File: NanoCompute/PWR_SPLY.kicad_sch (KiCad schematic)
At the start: 3 parts, among them U5 TPS54308, U7 TLV74311, U8 TLV74325

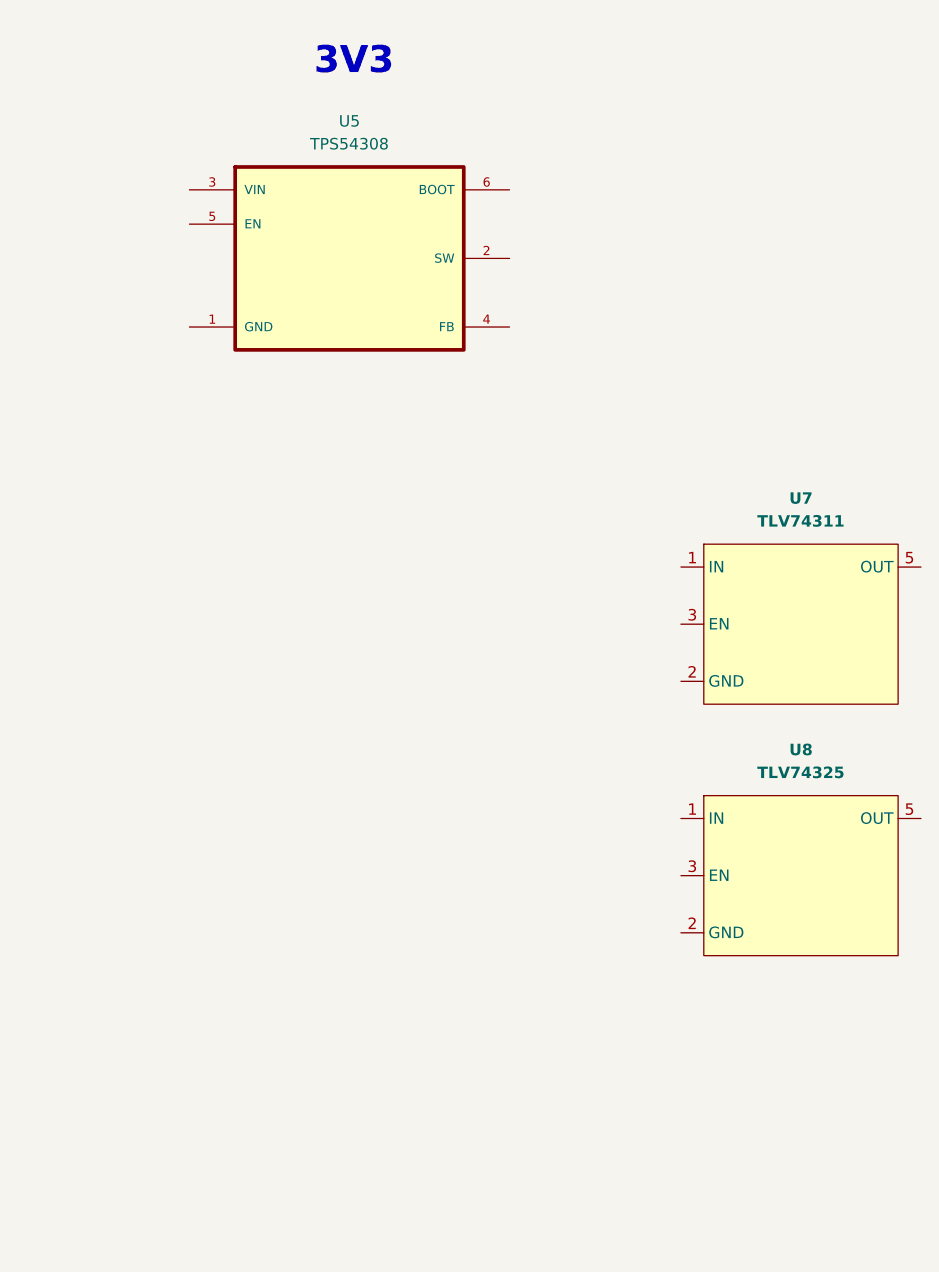
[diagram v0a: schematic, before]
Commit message: LPDDR4 second chip connected to LPDDR4 PHY
Added a missing Units for second LPDDR4 chip (VSS and Power).
Added a 1x100nF decoupling capacitor for each power rail of VDD1 but it
seems too much. Might need to find a better way of doing Low-Mid-High
range frequency decoupling.
Added TPS65296 as a LPddr4 Memory power solution but I need to check if
I can power both memory chips with just one TPS65296.
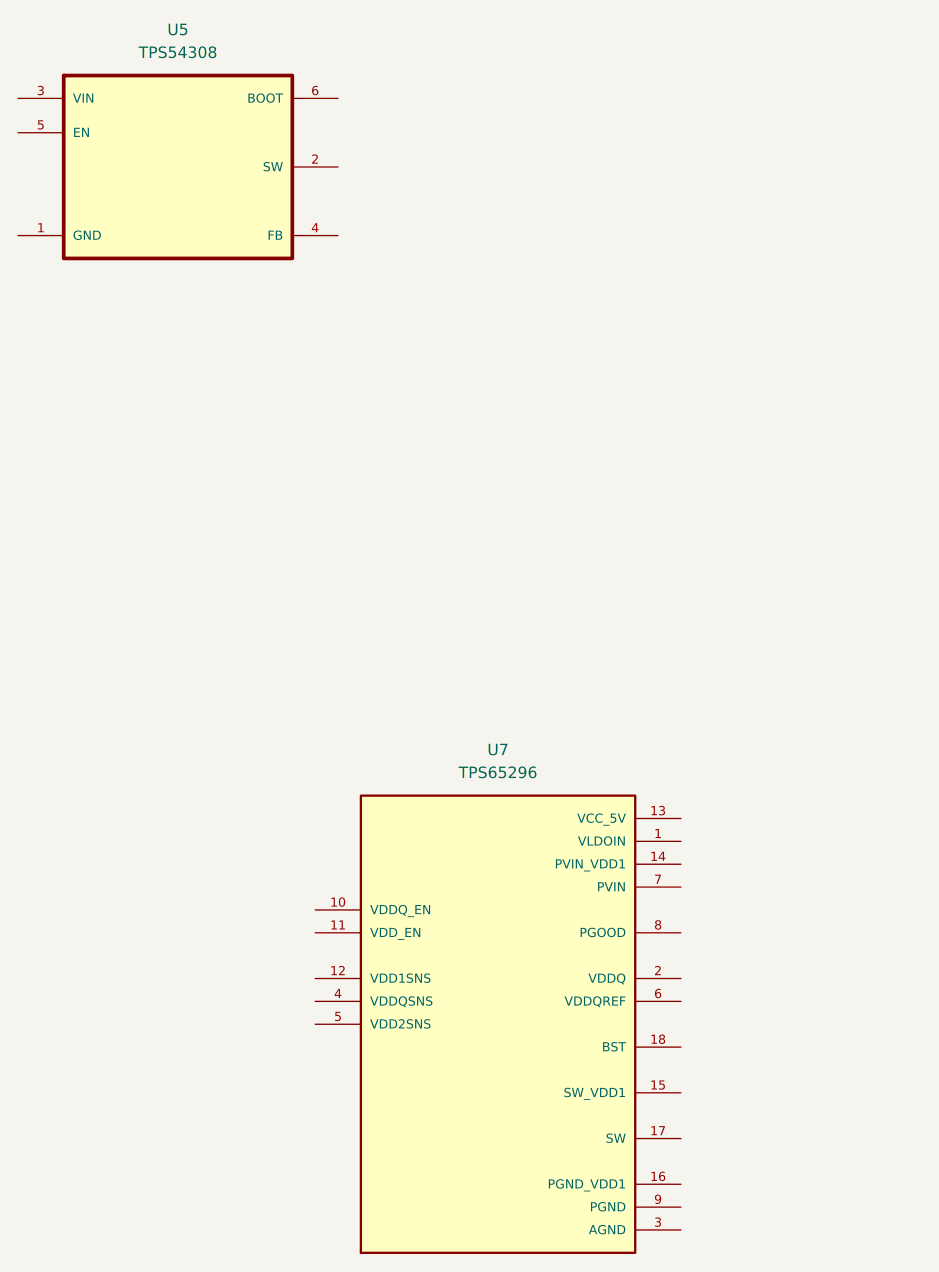
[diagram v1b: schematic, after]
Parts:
- removed U7: TLV74311, Package_TO_SOT_SMD:SOT-23-5, symbol CBSymLib:TLV743-11
- removed U8: TLV74325, Package_TO_SOT_SMD:SOT-23-5, symbol CBSymLib:TLV743-25
- added U7: TPS65296, CBFtLib:TPS65296RJER, symbol CBSymLib:TPS65296RJER
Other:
- note removed: "3V3"
- moved on the sheet: U5
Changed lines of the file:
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@@
 		(rev "v1.0")
 	)
-	(text "3V3"
-		(exclude_from_sim no)
-		(at 58.928 21.336 0)
-		(effects
-			(font
-				(size 3 3)
-				(thickness 0.6)
-				(bold yes)
-			)
-		)
-	)
 	(symbol
-		(lib_id "CBSymLib:TLV743-25")
-		(at 107.95 105.41 0)
+		(lib_id "CBSymLib:TPS65296RJER")
+		(at 74.93 128.27 0)
 		(unit 1)
 		(exclude_from_sim no)
@@
 		(on_board yes)
 		(dnp no)
-		(property "Reference" "U8"
-			(at 108.585 97.79 0)
+		(fields_autoplaced yes)
+		(property "Reference" "U7"
+			(at 74.93 97.79 0)
 			(effects
 				(font
 					(size 1.27 1.27)
-					(thickness 0.254)
-					(bold yes)
 				)
 			)
 		)
-		(property "Value" "TLV74325"
-			(at 108.585 100.33 0)
+		(property "Value" "TPS65296"
+			(at 74.93 100.33 0)
 			(effects
 				(font
 					(size 1.27 1.27)
-					(thickness 0.254)
-					(bold yes)
 				)
 			)
 		)
-		(property "Footprint" "Package_TO_SOT_SMD:SOT-23-5"
-			(at 107.95 105.41 0)
+		(property "Footprint" "CBFtLib:TPS65296RJER"
+			(at 74.93 128.27 0)
+			(effects
+				(font
+					(size 1.27 1.27)
+				)
+				(justify bottom)
+				(hide yes)
+			)
+		)
+		(property "Datasheet" "https://www.ti.com/general/docs/suppproductinfo.tsp?distId=10&gotoUrl=https%3A%2F%2Fwww.ti.com%2Flit%2Fgpn%2Ftps65296"
+			(at 74.93 128.27 0)
 			(effects
 				(font
@@
 			)
 		)
-		(property "Datasheet" "https://www.ti.com/general/docs/suppproductinfo.tsp?distId=10&gotoUrl=https%3A%2F%2Fwww.ti.com%2Flit%2Fgpn%2Ftlv743p"
-			(at 107.95 105.41 0)
+		(property "Description" "Converter, Notebook Power System Voltage Regulator IC 2 Output 18-VQFN-HR (3x3)"
+			(at 74.93 128.27 0)
 			(effects
 				(font
@@
 			)
 		)
-		(property "Description" "Linear Voltage Regulator IC Positive Fixed 1 Output 300mA SOT-23-5"
-			(at 107.95 105.41 0)
+		(property "Digikey stock" "5,921 - 4/1/2024"
+			(at 74.93 128.27 0)
 			(effects
 				(font
@@
 			)
 		)
-		(property "Digikey stock" "17,002 - 29/12/2024"
-			(at 107.95 105.41 0)
-			(effects
-				(font
-					(size 1.27 1.27)
-				)
-				(hide yes)
-			)
-		)
-		(property "MPN" "TLV74325PDBVR"
-			(at 107.95 105.41 0)
-			(effects
-				(font
-					(size 1.27 1.27)
-				)
-				(hide yes)
-			)
-		)
-		(pin "3"
-		)
-		(pin "1"
-		)
-		(pin "4"
-		)
-		(pin "5"
-		)
-		(pin "2"
-		)
-		(instances
-			(project "CuriosityBoard"
-				(path "/3a0a6fc3-d957-4804-b3c3-6d269c038b1f/d23503c1-e384-4c86-8da8-7bc1f5bc6ede"
-					(reference "U8")
-					(unit 1)
-				)
-			)
-		)
-	)
-	(symbol
-		(lib_id "CBSymLib:TLV743-11")
-		(at 107.95 77.47 0)
-		(unit 1)
-		(exclude_from_sim no)
-		(in_bom yes)
-		(on_board yes)
-		(dnp no)
-		(property "Reference" "U7"
-			(at 108.585 69.85 0)
-			(effects
-				(font
-					(size 1.27 1.27)
-					(thickness 0.254)
-					(bold yes)
-				)
-			)
-		)
-		(property "Value" "TLV74311"
-			(at 108.585 72.39 0)
-			(effects
-				(font
-					(size 1.27 1.27)
-					(thickness 0.254)
-					(bold yes)
-				)
-			)
-		)
-		(property "Footprint" "Package_TO_SOT_SMD:SOT-23-5"
-			(at 107.95 77.47 0)
-			(effects
-				(font
-					(size 1.27 1.27)
-				)
-				(hide yes)
-			)
-		)
-		(property "Datasheet" "https://www.ti.com/general/docs/suppproductinfo.tsp?distId=10&gotoUrl=https%3A%2F%2Fwww.ti.com%2Flit%2Fgpn%2Ftlv743p"
-			(at 107.95 77.47 0)
-			(effects
-				(font
-					(size 1.27 1.27)
-				)
-				(hide yes)
-			)
-		)
-		(property "Description" "Linear Voltage Regulator IC Positive Fixed 1 Output 300mA SOT-23-5"
-			(at 107.95 77.47 0)
-			(effects
-				(font
-					(size 1.27 1.27)
-				)
-				(hide yes)
-			)
-		)
-		(property "Digikey stock" "6,309 - 29/12/2024"
-			(at 107.95 77.47 0)
-			(effects
-				(font
-					(size 1.27 1.27)
-				)
-				(hide yes)
-			)
-		)
-		(property "MPN" "TLV74311PDBVR"
-			(at 107.95 77.47 0)
+		(property "MPN" "TPS65296RJER"
+			(at 74.93 128.27 0)
 			(effects
 				(font
@@
 		(pin "2"
 		)
+		(pin "18"
+		)
+		(pin "11"
+		)
+		(pin "16"
+		)
+		(pin "12"
+		)
+		(pin "4"
+		)
+		(pin "17"
+		)
 		(pin "5"
+		)
+		(pin "14"
+		)
+		(pin "7"
+		)
+		(pin "15"
+		)
+		(pin "13"
+		)
+		(pin "9"
+		)
+		(pin "8"
+		)
+		(pin "1"
 		)
 		(pin "3"
 		)
-		(pin "1"
+		(pin "6"
 		)
-		(pin "4"
+		(pin "10"
 		)
 		(instances
-			(project "CuriosityBoard"
+			(project ""
 				(path "/3a0a6fc3-d957-4804-b3c3-6d269c038b1f/d23503c1-e384-4c86-8da8-7bc1f5bc6ede"
 					(reference "U7")
@@
 	(symbol
 		(lib_id "CBSymLib:TPS54308DDCR")
-		(at 58.42 43.18 0)
+		(at 39.37 33.02 0)
 		(unit 1)
 		(exclude_from_sim no)
@@
 		(fields_autoplaced yes)
 		(property "Reference" "U5"
-			(at 58.42 27.94 0)
+			(at 39.37 17.78 0)
 			(effects
 				(font
@@
 		)
 		(property "Value" "TPS54308"
-			(at 58.42 30.48 0)
+			(at 39.37 20.32 0)
 			(effects
 				(font
@@
 		)
 		(property "Footprint" "CBFtLib:TPS54308DDCR"
-			(at 58.42 43.18 0)
+			(at 39.37 33.02 0)
 			(effects
 				(font
@@
 		)
 		(property "Datasheet" "https://www.ti.com/general/docs/suppproductinfo.tsp?distId=10&gotoUrl=https%3A%2F%2Fwww.ti.com%2Flit%2Fgpn%2Ftps54308"
-			(at 58.42 43.18 0)
+			(at 39.37 33.02 0)
 			(effects
 				(font
@@
 		)
 		(property "Description" "Buck Switching Regulator IC Positive Adjustable 1V 1 Output 3A SOT-23-6 Thin, TSOT-23-6"
-			(at 58.42 43.18 0)
+			(at 39.37 33.02 0)
 			(effects
 				(font
@@
 		)
 		(property "Digikey stock" "13,511 - 29/12/2024"
-			(at 58.42 43.18 0)
+			(at 39.37 33.02 0)
 			(effects
 				(font
@@
 		)
 		(property "MPN" "TPS54308DDCR"
-			(at 58.42 43.18 0)
+			(at 39.37 33.02 0)
 			(effects
 				(font

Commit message: Added eMMC 5.1 HS400 128GB
It would act as a on-board primary storage while NVMe would act as an
extension/upgrade.
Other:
- title: (none) -> NanoCompute
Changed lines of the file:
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@@
 	(paper "A4")
 	(title_block
-		(date "2025-01-01")
+		(title "NanoCompute")
+		(date "2025-01-06")
 		(rev "v1.0")
 	)
